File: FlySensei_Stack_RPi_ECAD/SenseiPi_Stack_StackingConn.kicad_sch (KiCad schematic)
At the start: 6 parts, among them J3 Conn_01x20_Female, J4 Conn_01x20_Male, J5 Conn_01x20_Female, J6 Conn_01x20_Male

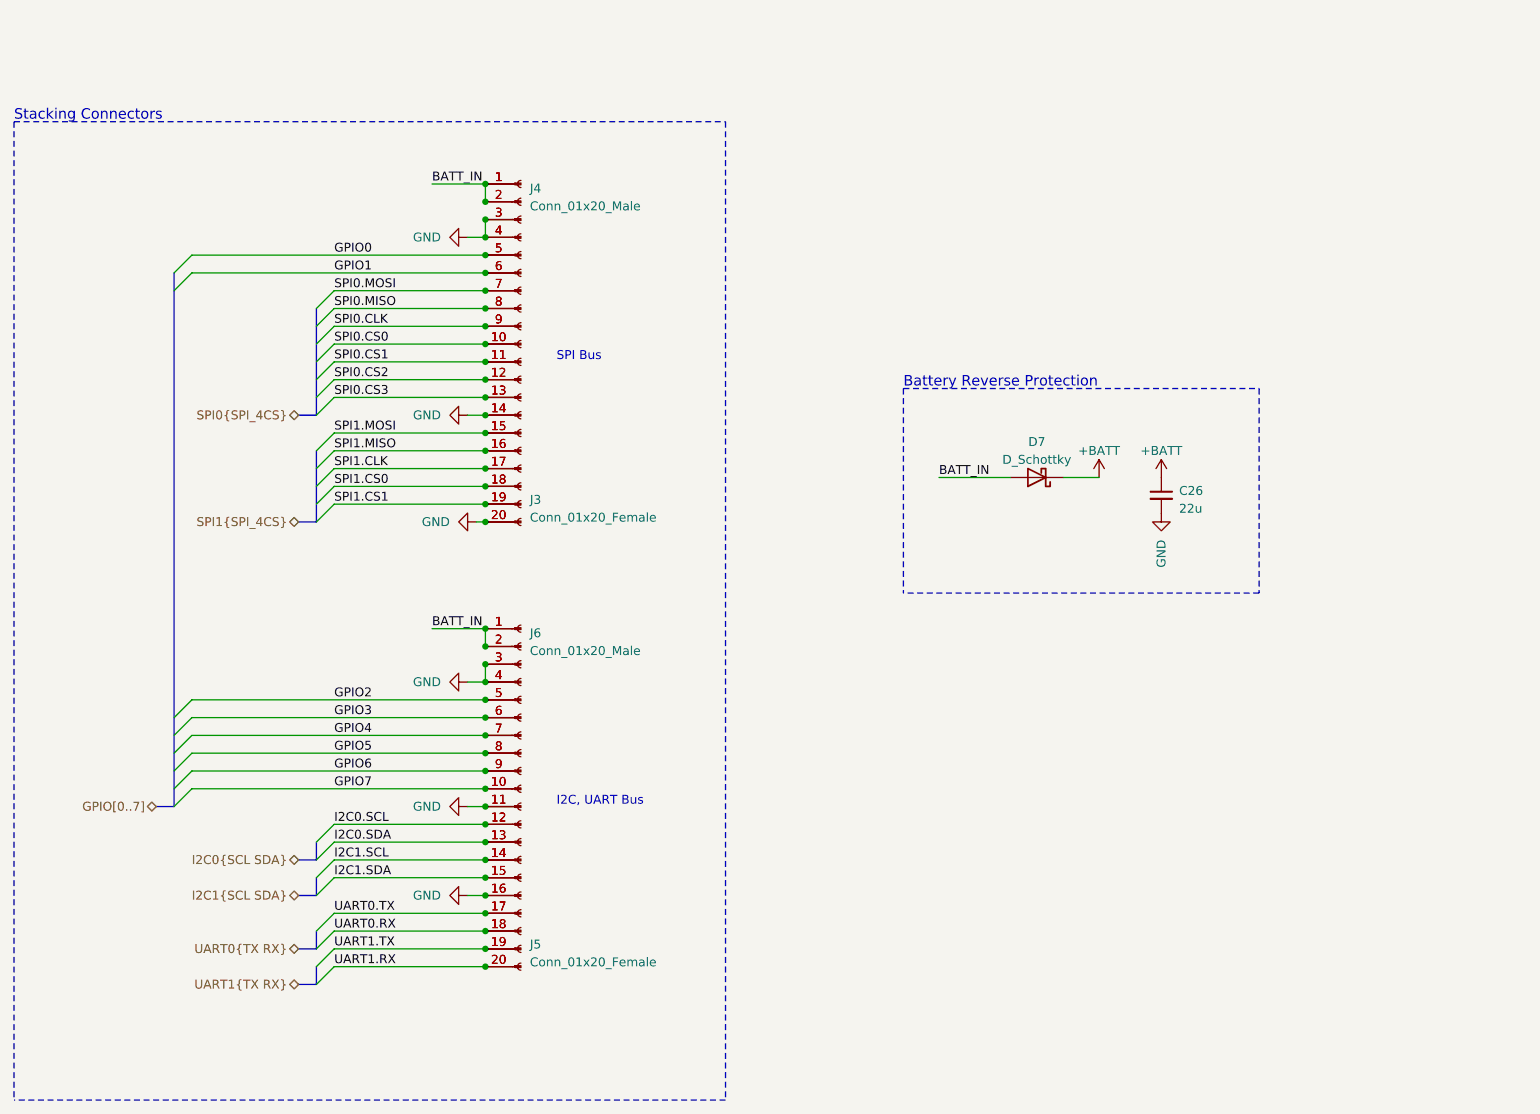
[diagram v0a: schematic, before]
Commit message: PCB Design for the Raspberry PI CM4 Board (V0.1)
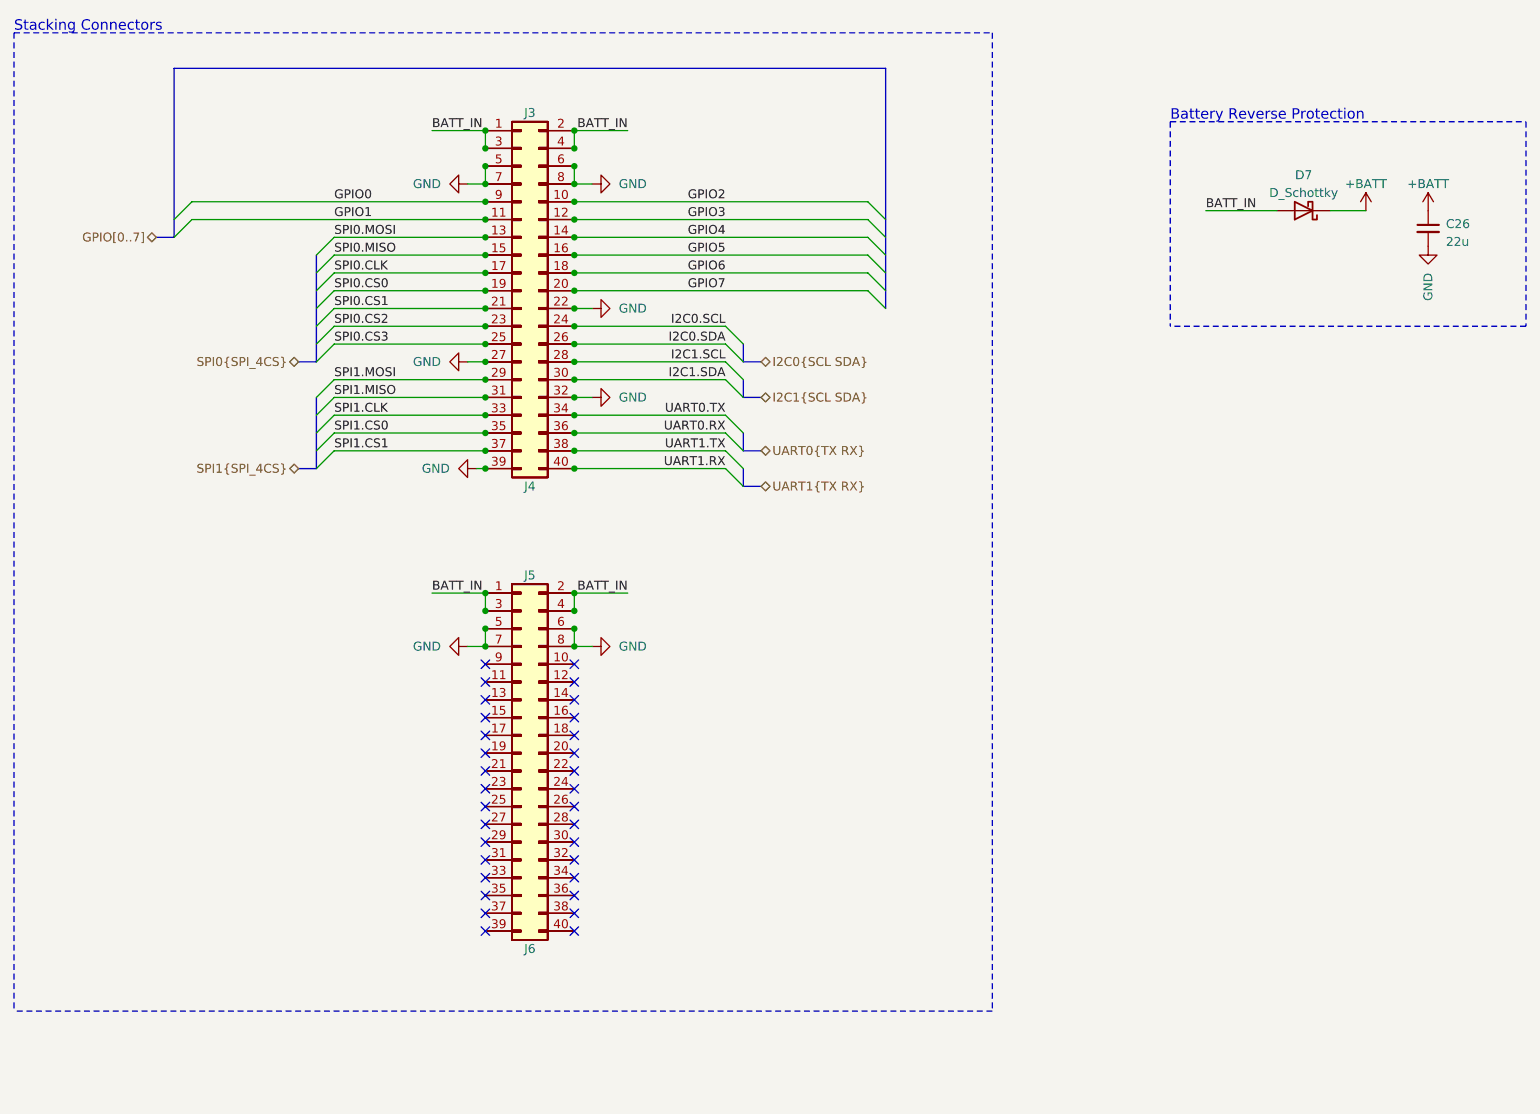
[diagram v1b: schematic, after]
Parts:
- removed J3, J5: Conn_01x20_Female, symbol Connector:Conn_01x20_Female
- removed J4, J6: Conn_01x20_Male, symbol Connector:Conn_01x20_Male
- added J3, J5: Conn_02x20_Odd_Even_Male, Connector_PinHeader_1.27mm:PinHeader_2x20_P1.27mm_Vertical_SMD, symbol Connector_Generic:Conn_02x20_Odd_Even
- added J4, J6: Conn_02x20_Odd_Even_Female, Connector_PinHeader_1.27mm:PinHeader_2x20_P1.27mm_Vertical_SMD, symbol Connector_Generic:Conn_02x20_Odd_Even
- C26: footprint (none) -> Capacitor_SMD:C_0805_2012Metric
- D7: footprint (none) -> Diode_SMD:D_SMB
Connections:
- net BATT_IN: now also J3.1 (Pin_1), J3.2 (Pin_2), J3.3 (Pin_3), J3.4 (Pin_4), J4.1 (Pin_1), J4.2 (Pin_2), J4.3 (Pin_3), J4.4 (Pin_4), J5.1 (Pin_1), J5.2 (Pin_2), J5.3 (Pin_3), J5.4 (Pin_4), J6.1 (Pin_1), J6.2 (Pin_2), J6.3 (Pin_3), J6.4 (Pin_4)
- net GND: now also J3.22 (Pin_22), J3.27 (Pin_27), J3.32 (Pin_32), J3.39 (Pin_39), J3.5 (Pin_5), J3.6 (Pin_6), J3.7 (Pin_7), J3.8 (Pin_8), J4.21 (Pin_21), J4.28 (Pin_28), J4.31 (Pin_31), J4.40 (Pin_40), J4.5 (Pin_5), J4.6 (Pin_6), J4.7 (Pin_7), J4.8 (Pin_8), J5.5 (Pin_5), J5.6 (Pin_6), J5.7 (Pin_7), J5.8 (Pin_8), J6.5 (Pin_5), J6.6 (Pin_6), J6.7 (Pin_7), J6.8 (Pin_8)
- net GPIO0: now also J3.9 (Pin_9), J4.10 (Pin_10)
- net GPIO1: now also J3.11 (Pin_11), J4.12 (Pin_12)
- net GPIO2: now also J3.10 (Pin_10), J4.9 (Pin_9)
- net GPIO3: now also J3.12 (Pin_12), J4.11 (Pin_11)
- net GPIO4: now also J3.14 (Pin_14), J4.13 (Pin_13)
- net GPIO5: now also J3.16 (Pin_16), J4.15 (Pin_15)
- net GPIO6: now also J3.18 (Pin_18), J4.17 (Pin_17)
- net GPIO7: now also J3.20 (Pin_20), J4.19 (Pin_19)
- net I2C0.SCL: now also J3.24 (Pin_24), J4.23 (Pin_23)
- net I2C0.SDA: now also J3.26 (Pin_26), J4.25 (Pin_25)
- net I2C1.SCL: now also J3.28 (Pin_28), J4.27 (Pin_27)
- net I2C1.SDA: now also J3.30 (Pin_30), J4.29 (Pin_29)
- net SPI0.CLK: now also J3.17 (Pin_17), J4.18 (Pin_18)
- net SPI0.CS0: now also J3.19 (Pin_19), J4.20 (Pin_20)
- net SPI0.CS1: now also J3.21 (Pin_21), J4.22 (Pin_22)
- net SPI0.CS2: now also J3.23 (Pin_23), J4.24 (Pin_24)
- net SPI0.CS3: now also J3.25 (Pin_25), J4.26 (Pin_26)
- net SPI0.MISO: now also J3.15 (Pin_15), J4.16 (Pin_16)
- net SPI0.MOSI: now also J3.13 (Pin_13), J4.14 (Pin_14)
- net SPI1.CLK: now also J3.33 (Pin_33), J4.34 (Pin_34)
- net SPI1.CS0: now also J3.35 (Pin_35), J4.36 (Pin_36)
- net SPI1.CS1: now also J3.37 (Pin_37), J4.38 (Pin_38)
- net SPI1.MISO: now also J3.31 (Pin_31), J4.32 (Pin_32)
- net SPI1.MOSI: now also J3.29 (Pin_29), J4.30 (Pin_30)
- net UART0.RX: now also J3.36 (Pin_36), J4.35 (Pin_35)
- net UART0.TX: now also J3.34 (Pin_34), J4.33 (Pin_33)
- net UART1.RX: now also J3.40 (Pin_40), J4.39 (Pin_39)
- net UART1.TX: now also J3.38 (Pin_38), J4.37 (Pin_37)
- new net: J5.9 (Pin_9), J6.10 (Pin_10)
- new net: J5.12 (Pin_12), J6.11 (Pin_11)
- new net: J5.11 (Pin_11), J6.12 (Pin_12)
- new net: J5.14 (Pin_14), J6.13 (Pin_13)
- new net: J5.13 (Pin_13), J6.14 (Pin_14)
- new net: J5.16 (Pin_16), J6.15 (Pin_15)
- new net: J5.15 (Pin_15), J6.16 (Pin_16)
- new net: J5.18 (Pin_18), J6.17 (Pin_17)
- new net: J5.17 (Pin_17), J6.18 (Pin_18)
- new net: J5.20 (Pin_20), J6.19 (Pin_19)
- new net: J5.19 (Pin_19), J6.20 (Pin_20)
- new net: J5.22 (Pin_22), J6.21 (Pin_21)
- new net: J5.21 (Pin_21), J6.22 (Pin_22)
- new net: J5.24 (Pin_24), J6.23 (Pin_23)
- new net: J5.23 (Pin_23), J6.24 (Pin_24)
- new net: J5.26 (Pin_26), J6.25 (Pin_25)
- new net: J5.25 (Pin_25), J6.26 (Pin_26)
- new net: J5.28 (Pin_28), J6.27 (Pin_27)
- new net: J5.27 (Pin_27), J6.28 (Pin_28)
- new net: J5.30 (Pin_30), J6.29 (Pin_29)
- new net: J5.29 (Pin_29), J6.30 (Pin_30)
- new net: J5.32 (Pin_32), J6.31 (Pin_31)
- new net: J5.31 (Pin_31), J6.32 (Pin_32)
- new net: J5.34 (Pin_34), J6.33 (Pin_33)
- new net: J5.33 (Pin_33), J6.34 (Pin_34)
- new net: J5.36 (Pin_36), J6.35 (Pin_35)
- new net: J5.35 (Pin_35), J6.36 (Pin_36)
- new net: J5.38 (Pin_38), J6.37 (Pin_37)
- new net: J5.37 (Pin_37), J6.38 (Pin_38)
- new net: J5.40 (Pin_40), J6.39 (Pin_39)
- new net: J5.39 (Pin_39), J6.40 (Pin_40)
- new net: J5.10 (Pin_10), J6.9 (Pin_9)
- no-connect marks 0 -> 32
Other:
- note removed: "I2C, UART Bus"
- note removed: "SPI Bus"
- moved on the sheet: C26, D7
